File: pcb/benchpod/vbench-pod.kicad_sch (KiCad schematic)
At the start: 110 parts, among them J1 PZ254V-12-22P, SW1 TS-1088-AR02016, SW2 TS-1088-AR02016, U1 ICE40UP5K-SG48ITR, U10 TCAN1044VDRBRQ1, U2 W25Q64JVSSIQ, U24 SN74LVC2G66DCUR, U28 SRV05-4.TCT, U4 ESP32-C3-MINI-1-N4, U5 STM32H563ZGT6, U7 APS6404L-3SQR-ZR, U8 TPS2116DRLR, X1 SX3M48.000B10F20TNN, Y2 6pF ±10ppm SMD2016-4P Crystal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

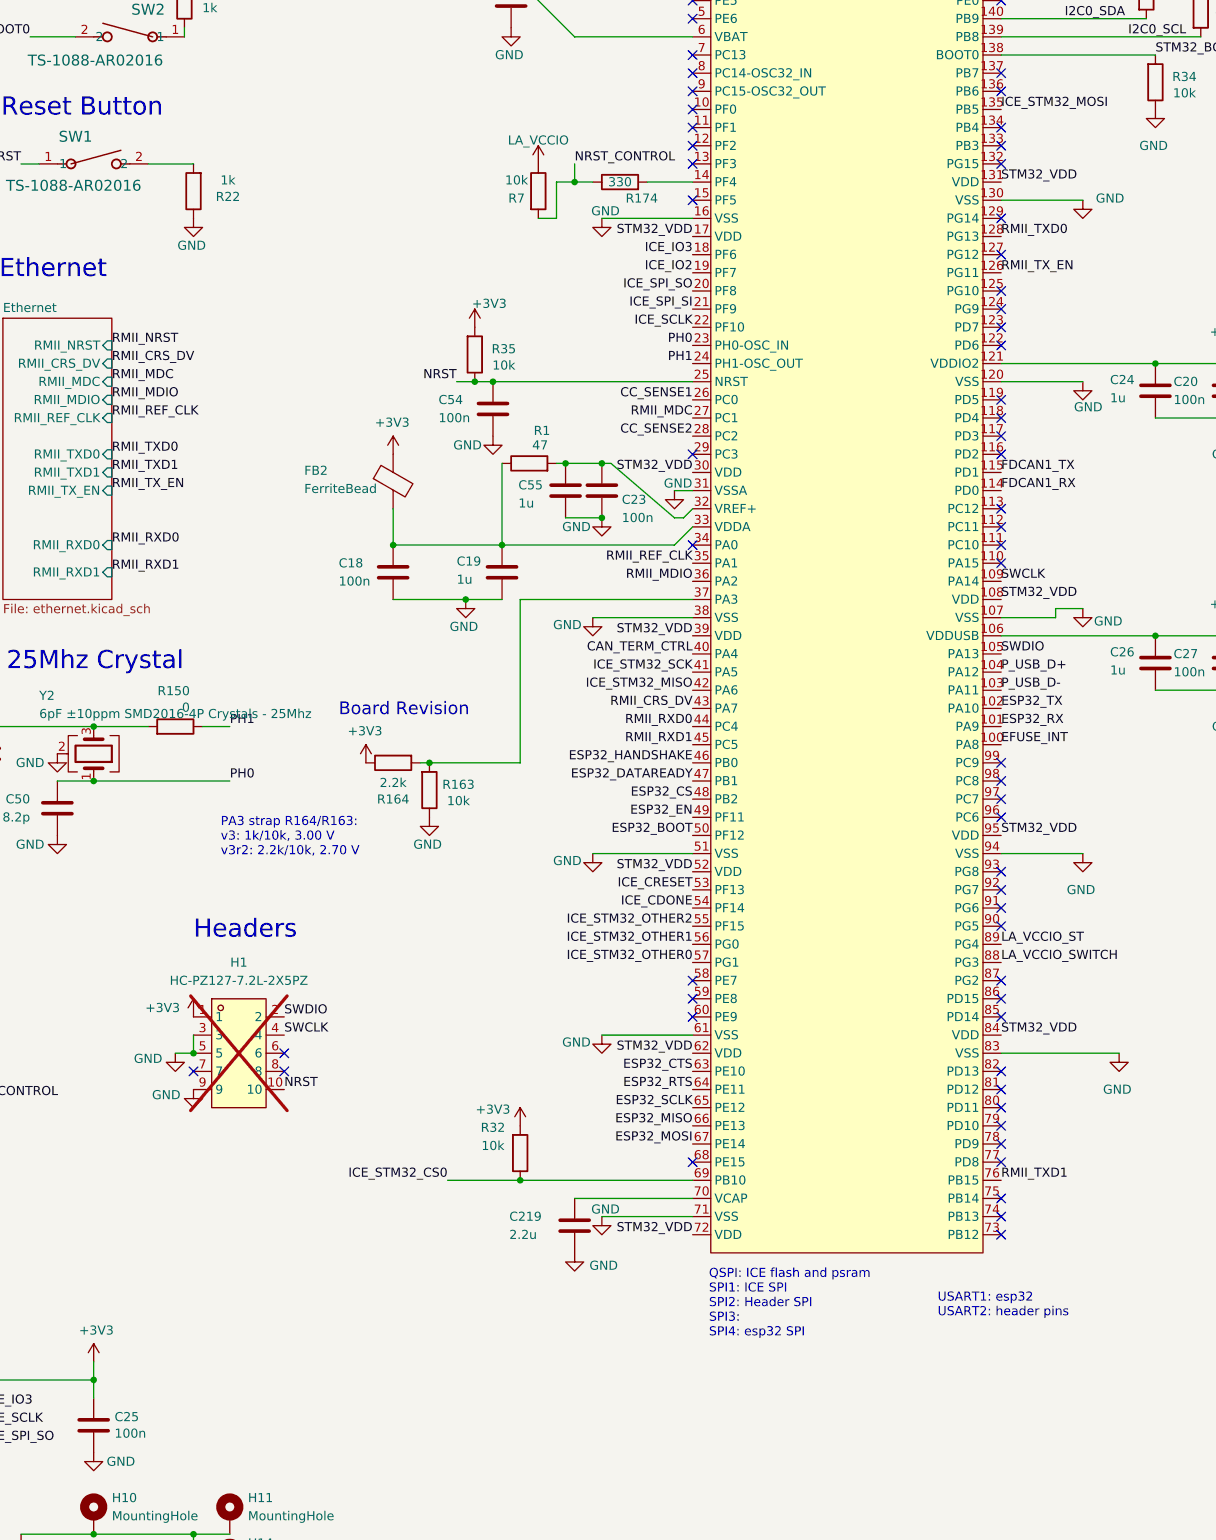
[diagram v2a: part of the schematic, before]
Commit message: analog v3r2: SWD on a TC2030 footprint with SWO, USART2 console on test pads
- H1 (2x5 1.27 mm SWD header, DNP) -> J10 Tag-Connect TC2030-IDC footprint
  (Connector:Tag-Connect_TC2030-IDC-FP_2x03_P1.27mm_Vertical, legged):
  VCC=+3V3, SWDIO, NRST, SWCLK, GND, and pin 6 SWO = PB3 (was unused).
  TC2030-IDC plugs into a 10-pin Cortex debug header.
- USART2 (PD5 TX, PD6 RX), the firmware's mirrored console, on test pads
  TP8 (TX), TP9 (RX) and TP10 (GND), 1.5 mm pads, in place of H2's pins.
- J10 and the pads are footprints only (in_bom no, like TP3/TP7).

ERC: one extra pin_not_driven on J10 SWO (STM32 pins have no pin type).
BOM lines unchanged (123).

Co-Authored-By: Claude Opus 5.5 <noreply@anthropic.com>
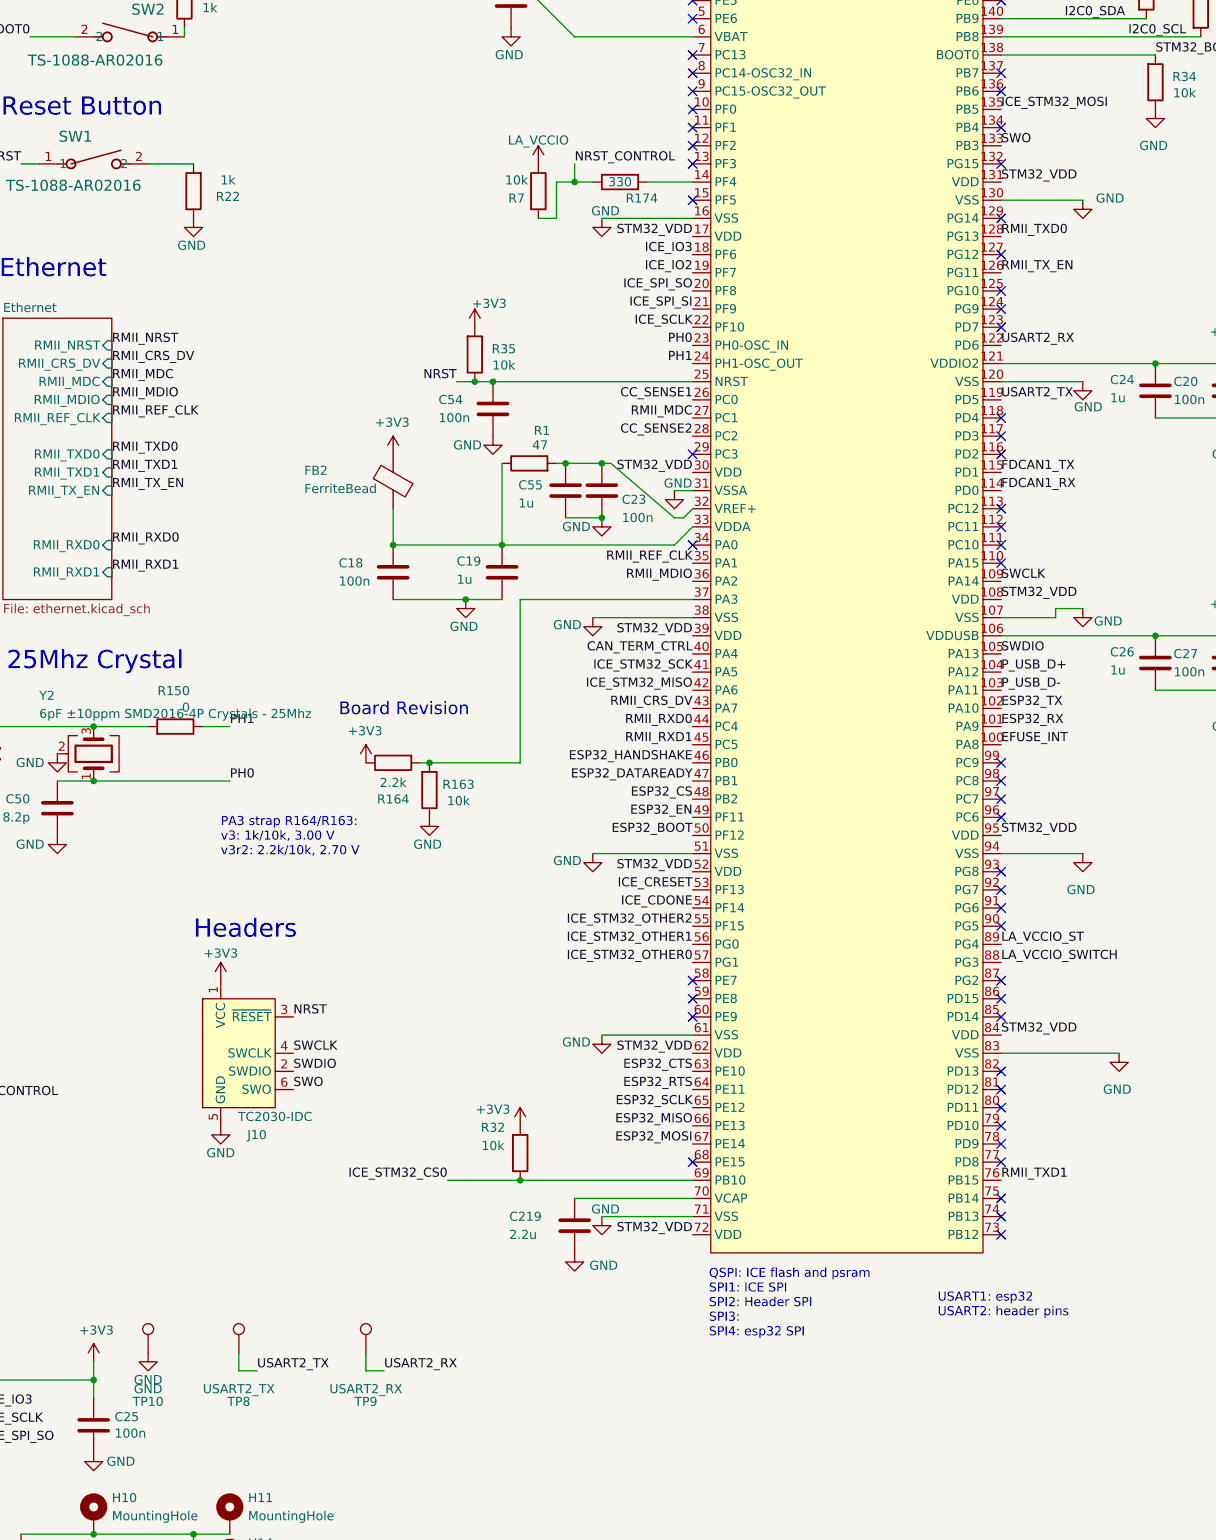
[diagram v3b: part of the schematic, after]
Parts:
- removed H1: HC-PZ127-7.2L-2X5PZ, lcsc:HDR-TH_HC-PZ127-7.2L-2X5PZ, symbol lcsc_lib:HC-PZ127-7.2L-2X5PZ
- added J10: TC2030-IDC, Connector:Tag-Connect_TC2030-IDC-FP_2x03_P1.27mm_Vertical, symbol Connector:Conn_ARM_SWD_TagConnect_TC2030
- added TP10: GND, TestPoint:TestPoint_Pad_1.5x1.5mm, symbol Connector:TestPoint
- added TP8: USART2_TX, TestPoint:TestPoint_Pad_1.5x1.5mm, symbol Connector:TestPoint
- added TP9: USART2_RX, TestPoint:TestPoint_Pad_1.5x1.5mm, symbol Connector:TestPoint
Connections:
- net +3V3: now also J10.1 (VCC)
- net GND: now also J10.5 (GND), TP10.1
- net NRST: now also J10.3 (~{RESET})
- net SWCLK: now also J10.4 (SWCLK)
- net SWDIO: now also J10.2 (SWDIO)
- net USART2_TX: now reaches U5.119 (PD5)
- net USART2_TX: now also TP8.1
- net USART2_RX: now reaches U5.122 (PD6)
- net USART2_RX: now also TP9.1
- net SWO: now reaches U5.133 (PB3)
- net SWO: now also J10.6 (SWO)
- no-connect marks 77 -> 71

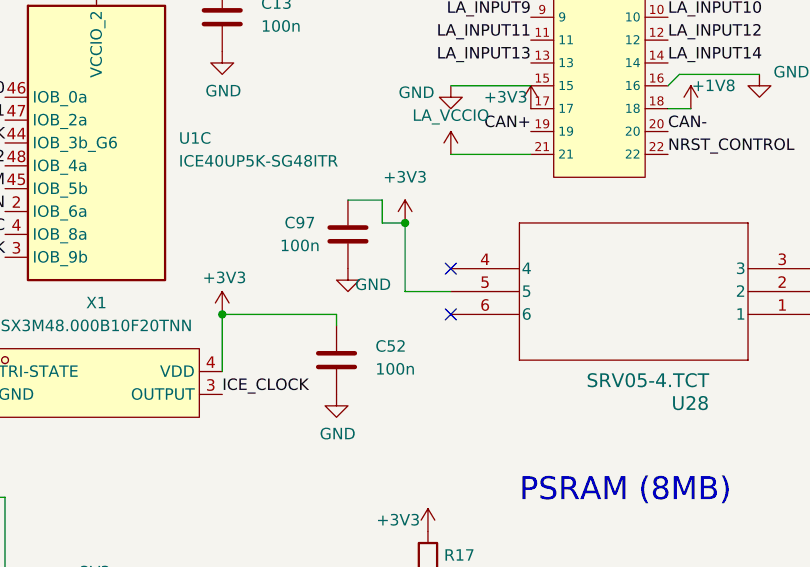
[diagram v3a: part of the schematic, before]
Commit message: analog v3r2: EMC pre-scan fixes in the schematic, no new BOM lines
From compliance emc/prescan-2026-10-18.md (schematic part; layout is separate):
- C267 100 nF (C307331) at U37 (THS4551) pin 5 VS-; C224/C157 sit at the
  LM7705 on the power sheet, not at the driver.
- USB-C CC1/CC2 clamped by the two unused channels of D11 (USBLC6-4, pins
  6 and 4), which already protects D+/D-.
- LA header +1V8 (J1.18) and LA_VCCIO (J1.21) on the two unused channels of
  U28 (SRV05-4, pins 4 and 6); +3V3 (J1.17) is U28's own VDD rail, so it is
  clamped by U28 already. Layout: U28 next to J1.
- RF2 (0-5 V SMA) gets D21 SMF13CA (C1851355, same as D19/D20): the jack had
  no clamp of its own and floats behind K1 during cal1.
- CAN needs nothing: TCAN1044V is rated +-8 kV contact / +-15 kV air
  (system level) on CANH/CANL, plus the 56 ohm series resistors.

Netlist diff = exactly these connections; no field moves; ERC errors
unchanged (26); BOM 123 lines.

Co-Authored-By: Claude Opus 5.5 <noreply@anthropic.com>
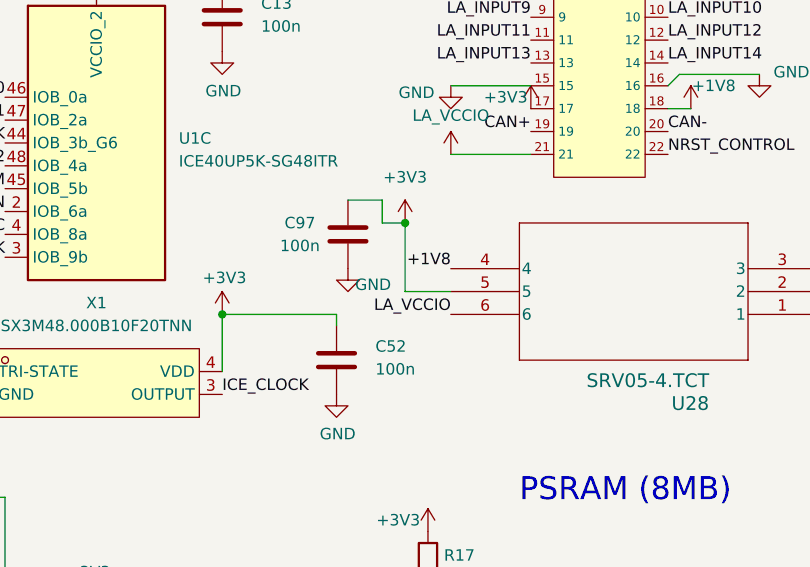
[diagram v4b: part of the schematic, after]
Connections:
- net +1V8: now also U28.4
- net LA_VCCIO: now also U28.6
- no-connect marks 71 -> 69
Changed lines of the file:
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@@
 	)
 	(no_connect
-		(at 184.15 214.63)
-	)
-	(no_connect
 		(at 373.38 170.18)
 	)
 	(no_connect
-		(at 184.15 219.71)
-	)
-	(no_connect
 		(at 373.38 78.74)
 	)
@@
 		)
 	)
+	(label "LA_VCCIO"
+		(at 184.15 219.71 180)
+		(effects
+			(font
+				(size 1.27 1.27)
+			)
+			(justify right bottom)
+		)
+	)
 	(label "ICE_SS_PSRAM"
 		(at 170.18 255.27 180)
@@
 		)
 	)
+	(label "+1V8"
+		(at 184.15 214.63 180)
+		(effects
+			(font
+				(size 1.27 1.27)
+			)
+			(justify right bottom)
+		)
+	)
